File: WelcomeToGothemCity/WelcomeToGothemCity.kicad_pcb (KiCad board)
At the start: 8 copper layers, 179 x 47 mm, 4 parts

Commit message: Complete Welcome To Gothem City
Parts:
- added P1: HC-SR04, PIN_ARRAY_4x1, F.Cu at (113.0, 63.5)
- added P2: LEDS, PIN_ARRAY_2X1, F.Cu at (102.9, 86.4)
- added P3: CONN_1, PIN_ARRAY_1, F.Cu at (200.7, 99.1)
- added P4: CONN_1, PIN_ARRAY_1, F.Cu at (195.6, 96.5)
- added P5: CONN_1, PIN_ARRAY_1, F.Cu at (195.6, 94.0)
- added Q1: TIP120, TO220_VERT, F.Cu at (116.8, 86.4)
- added R1: 1K Ohms, R4, F.Cu at (124.5, 91.4)
- added R2: R, R4, F.Cu at (109.2, 91.4)
- added U1: ADAFRUIT_POWERBOOST_500, PBost500Breakout, F.Cu at (142.2, 75.6)
- added U2: METROMINI, MetroMini, F.Cu at (184.2, 76.2)
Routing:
- net (no net): track 2486.7 -> 1333.5 mm, vias 1236 -> 753
- net GND: track 0.00 -> 444.7 mm, vias 0 -> 155
- net +BATT: track 0.00 -> 406.8 mm, vias 0 -> 138
- net +5V: track 0.00 -> 391.5 mm, vias 0 -> 130
- net N-0000010: track 0.00 -> 110.1 mm, vias 0 -> 10
- net /Echo: track 0.00 -> 90.1 mm, vias 0 -> 10
- net /Trig: track 0.00 -> 90.0 mm, vias 0 -> 10
- net N-000002: track 0.00 -> 69.6 mm, vias 0 -> 10
- net N-000009: track 0.00 -> 20.3 mm, vias 0 -> 10
- net N-000007: track 0.00 -> 10.2 mm, vias 0 -> 5
- net N-000006: track 0.00 -> 10.2 mm, vias 0 -> 5

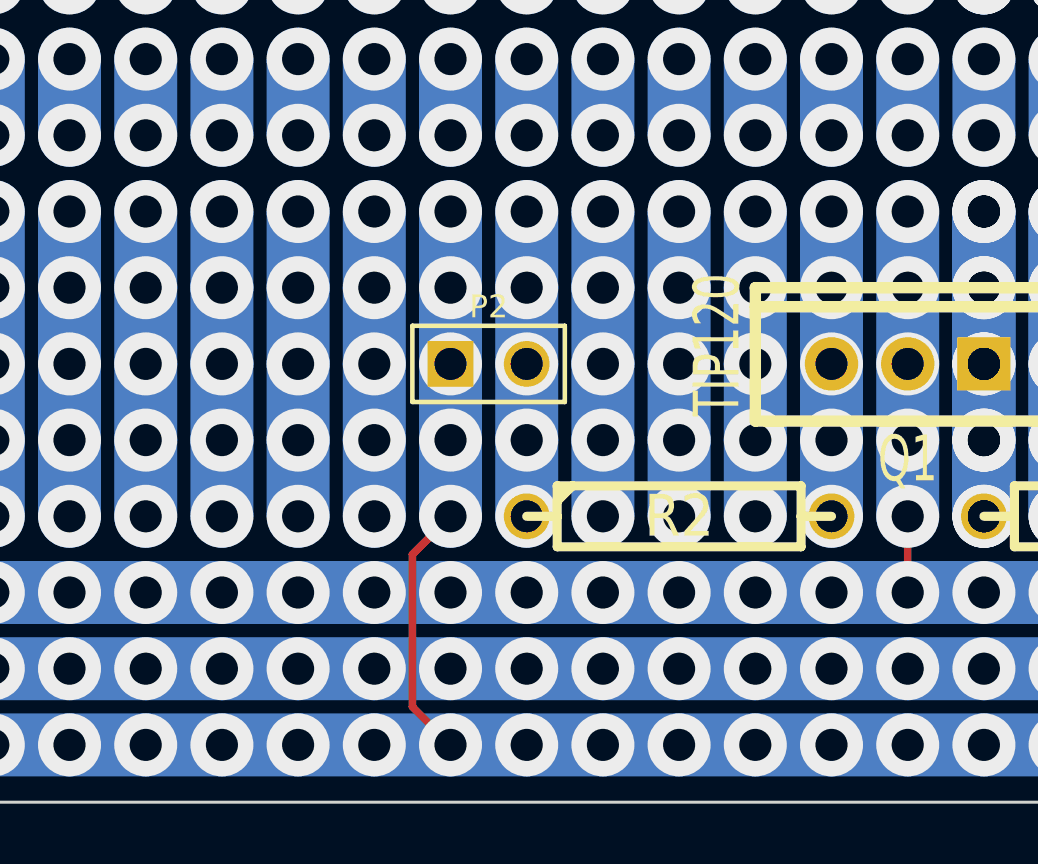
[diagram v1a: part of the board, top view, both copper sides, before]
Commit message: Update WelcomeToGothemCity: actual value for R2
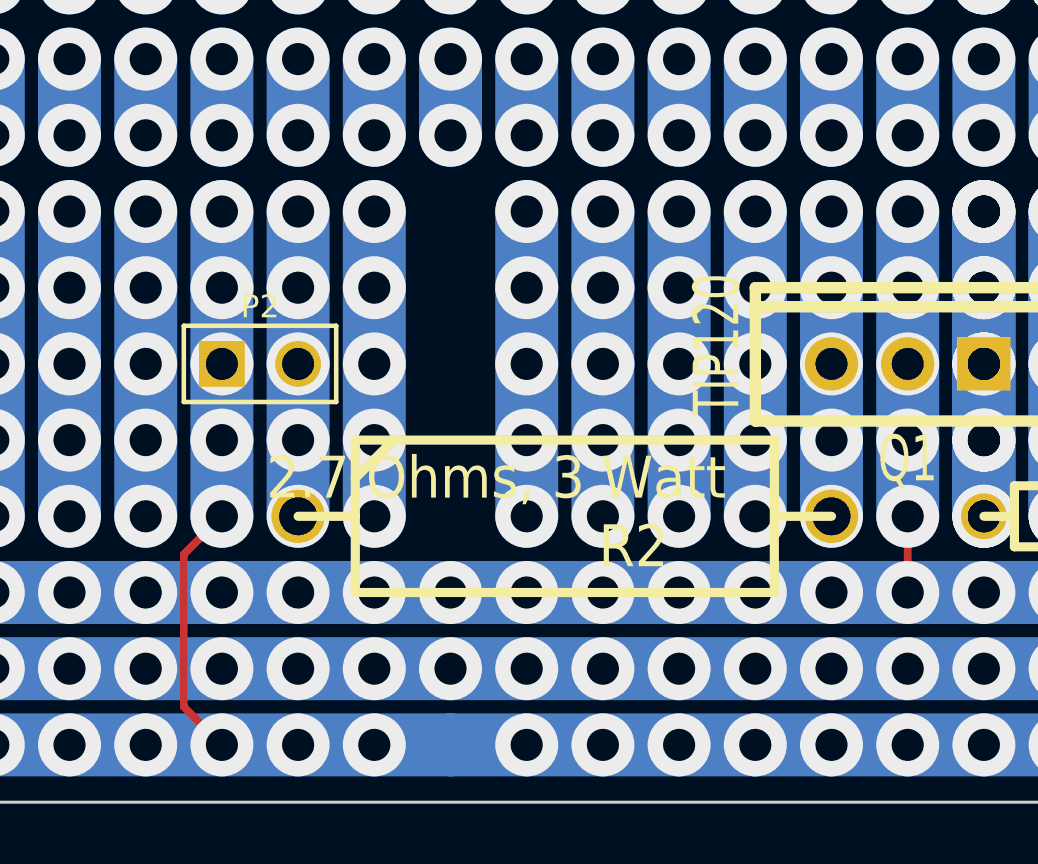
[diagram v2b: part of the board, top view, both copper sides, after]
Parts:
- R2: value R -> 2.7 Ohms, 3 Watt; footprint R4 -> R7
- moved P2 7.62 mm to (95.2, 86.4)
- moved R2 3.81 mm to (105.4, 91.4)
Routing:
- net (no net): track 1333.5 -> 1323.3 mm, vias 753 -> 748
- net +BATT: vias 138 -> 137

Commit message: Minor fixes to WelcomeToGothemCity PCB
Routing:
- net (no net): track 1323.3 -> 1333.5 mm, vias 748 -> 753
- net +BATT: vias 137 -> 138
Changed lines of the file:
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@@
     (links 18)
     (no_connects 0)
-    (area 31.099999 53.919999 210.200001 101.020001)
+    (area 31.099999 53.78 210.200001 101.160001)
     (thickness 1.6)
     (drawings 4)
-    (tracks 2263)
+    (tracks 2273)
     (zones 0)
     (modules 14)
@@
     (2 Inner2.Cu signal)
     (1 Inner1.Cu signal)
-    (0 B.Cu signal hide)
+    (0 B.Cu signal)
     (16 B.Adhes user)
     (17 F.Adhes user)
@@
   (gr_line (start 210.15 53.97) (end 210.15 100.97) (angle 90) (layer Edge.Cuts) (width 0.1))
   (gr_line (start 31.15 53.97) (end 210.15 53.97) (angle 90) (layer Edge.Cuts) (width 0.1))
+  (segment (start 101.6 83.82) (end 101.6 86.36) (width 2.1) (layer B.Cu) (net 0))
+  (segment (start 101.6 83.82) (end 101.6 81.28) (width 2.1) (layer B.Cu) (net 0))
+  (via (at 101.6 91.44) (size 2.1) (drill 1.07) (layers F.Cu B.Cu) (net 0))
+  (segment (start 101.6 91.44) (end 101.6 88.9) (width 2.1) (layer B.Cu) (net 0))
+  (segment (start 101.6 86.36) (end 101.6 88.9) (width 2.1) (layer B.Cu) (net 0))
+  (via (at 101.6 81.28) (size 2.1) (drill 1.07) (layers F.Cu B.Cu) (net 0))
+  (via (at 101.6 83.82) (size 2.1) (drill 1.07) (layers F.Cu B.Cu) (net 0))
+  (via (at 101.6 86.36) (size 2.1) (drill 1.07) (layers F.Cu B.Cu) (net 0))
+  (via (at 101.6 88.9) (size 2.1) (drill 1.07) (layers F.Cu B.Cu) (net 0))
   (via (at 127 88.9) (size 2.1) (drill 1.07) (layers F.Cu B.Cu) (net 0))
   (via (at 127 86.36) (size 2.1) (drill 1.07) (layers F.Cu B.Cu) (net 0))
@@
   (via (at 109.22 68.58) (size 2.1) (drill 1.07) (layers F.Cu B.Cu) (net 1))
   (via (at 109.22 71.12) (size 2.1) (drill 1.07) (layers F.Cu B.Cu) (net 1))
+  (via (at 101.6 99.06) (size 2.1) (drill 1.07) (layers F.Cu B.Cu) (net 2))
   (segment (start 93.98 91.44) (end 92.71 92.71) (width 0.254) (layer F.Cu) (net 2))
   (via (at 93.98 99.06) (size 2.1) (drill 1.07) (layers F.Cu B.Cu) (net 2))

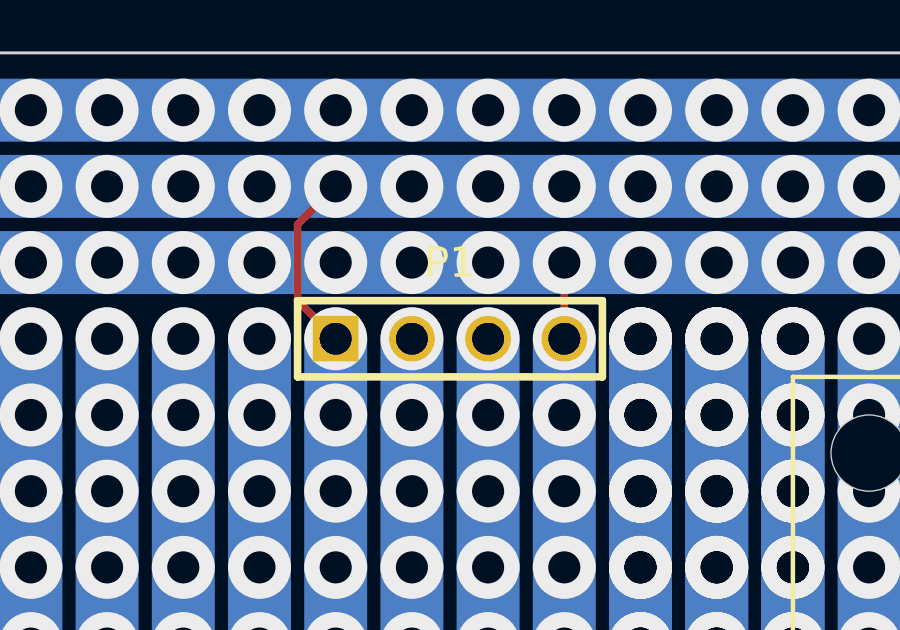
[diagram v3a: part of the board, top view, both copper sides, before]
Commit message: Update WelcomeToGothemCity PCB (correct orientation of SR04 connector).
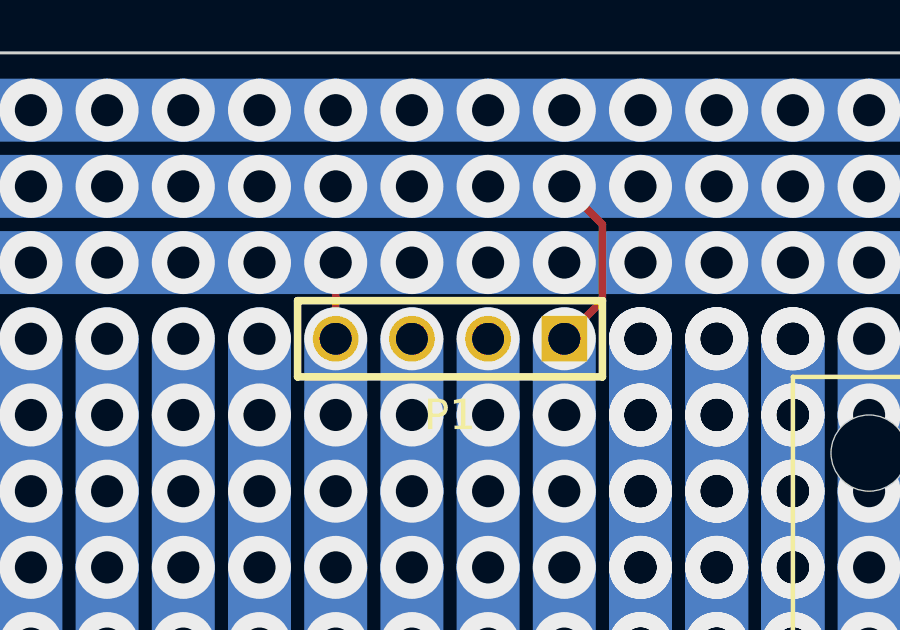
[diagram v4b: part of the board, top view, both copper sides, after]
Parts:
- turned P1 to 180 degrees
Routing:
- net /Echo: track 90.1 -> 92.7 mm
- net /Trig: track 90.0 -> 87.4 mm

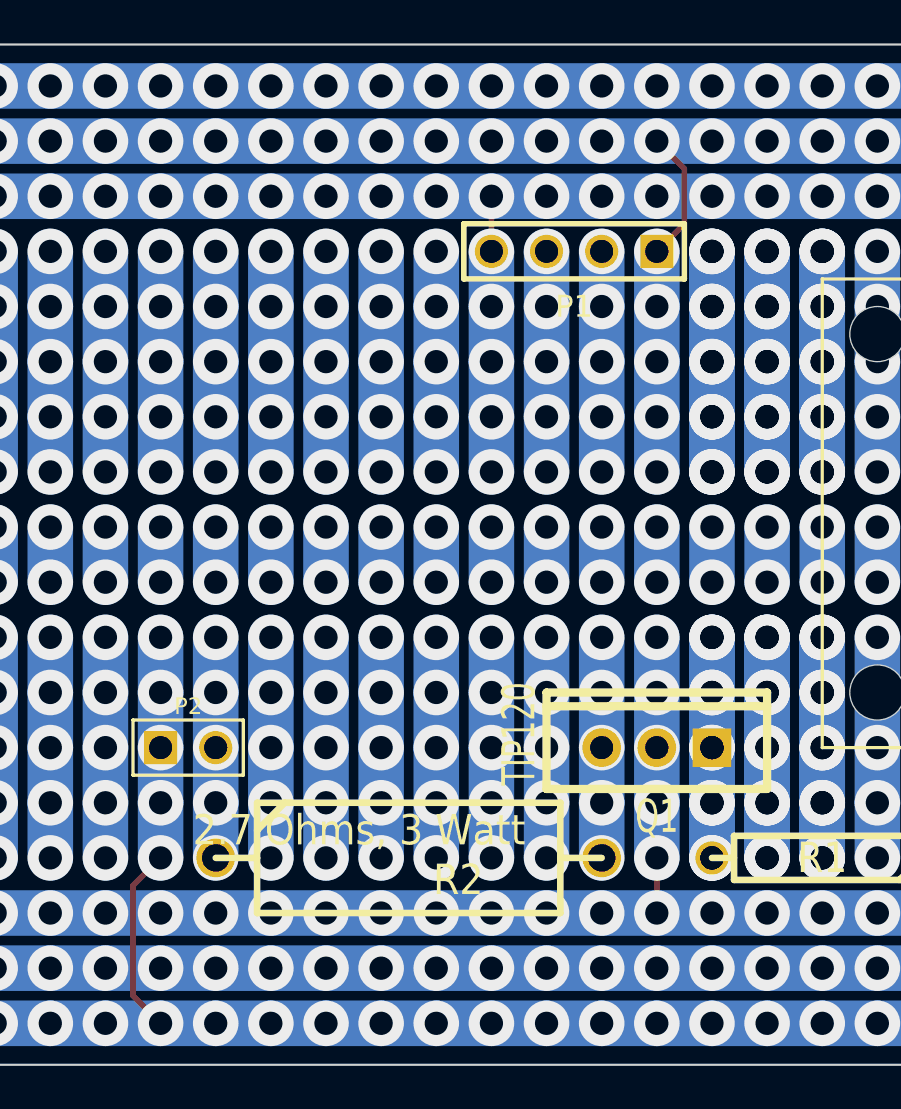
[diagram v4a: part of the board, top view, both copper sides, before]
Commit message: Fix transistor module (correct pin ordering).
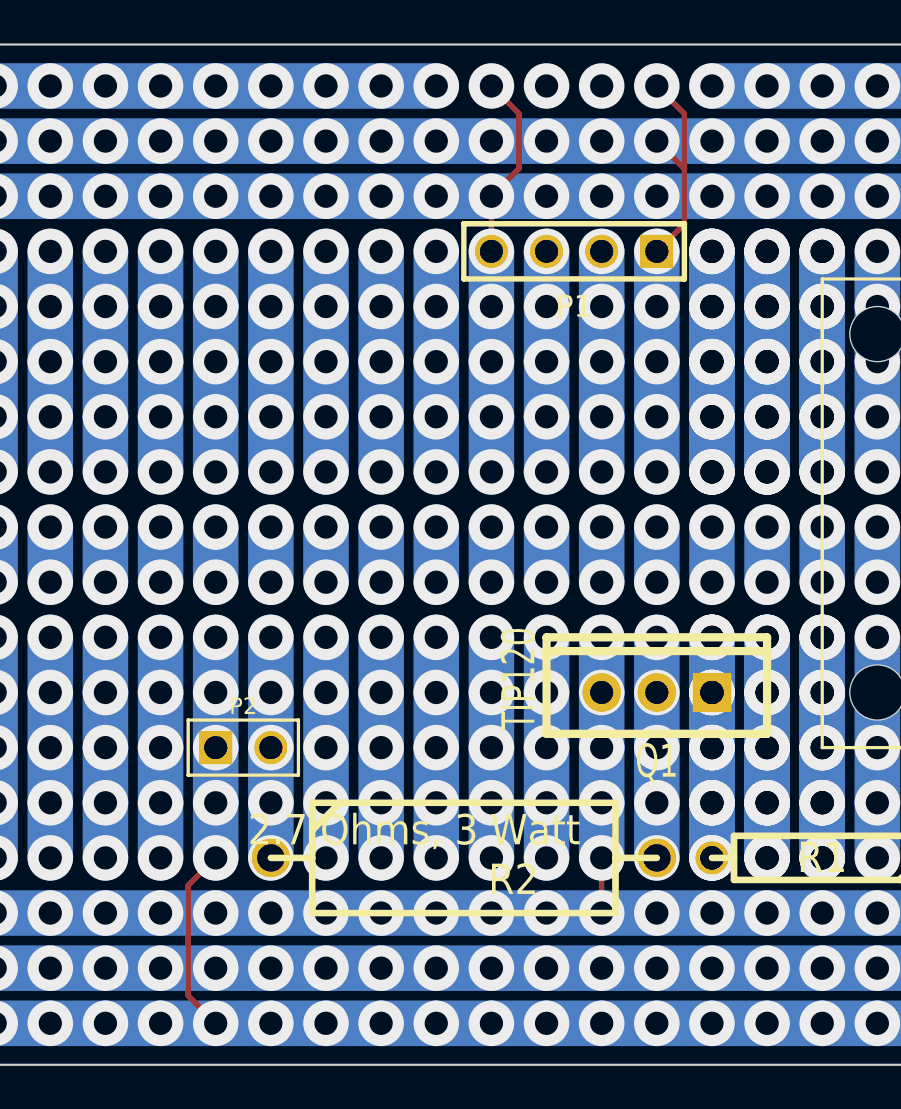
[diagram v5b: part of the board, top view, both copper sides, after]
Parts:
- Q1: footprint TO220_VERT -> TO220_VERT_tip120
- moved P2 2.54 mm to (97.8, 86.4)
- moved Q1 2.54 mm to (116.8, 83.8)
- moved R2 2.54 mm to (108.0, 91.4)
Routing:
- net +BATT: track 406.8 -> 338.2 mm, vias 138 -> 112
- net (no net): track 1333.5 -> 1389.4 mm, vias 753 -> 775
- net /Trig: track 87.4 -> 96.1 mm, vias 10 -> 11
- net /Echo: track 92.7 -> 99.6 mm, vias 10 -> 11
- net GND: track 444.7 -> 450.8 mm, vias 155 -> 156
- net +5V: track 391.5 -> 395.8 mm, vias 130 -> 131
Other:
- board text added: "1"
- board text added: "1 0"
- board text added: "1 1"
- board text added: "1 2"
- board text added: "1 3"
- board text added: "1 4"
- board text added: "1 5"
- board text added: "1 6"
- board text added: "1 7"
- board text added: "1 8"
- board text added: "1 9"
- board text added: "2"
- board text added: "2 0"
- board text added: "2 1"
- board text added: "2 2"
- board text added: "2 3"
- board text added: "2 4"
- board text added: "2 5"
- board text added: "2 6"
- board text added: "2 7"
- board text added: "2 8"
- board text added: "2 9"
- board text added: "3"
- board text added: "3 0"
- board text added: "3 1"
- board text added: "3 2"
- board text added: "3 3"
- board text added: "3 4"
- board text added: "3 5"
- board text added: "3 6"
- board text added: "3 7"
- board text added: "3 8"
- board text added: "3 9"
- board text added: "4"
- board text added: "4 0"
- board text added: "5"
- board text added: "6"
- board text added: "7"
- board text added: "8"
- board text added: "9"
